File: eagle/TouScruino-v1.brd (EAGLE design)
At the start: 53.3 x 59.7 mm, 47 parts, among them J1 AVR_ISP, Q1 8MHz, Q2 MMBT2222, Q3 8MHz, U1 ATMEGA1284P, U3 ARDUINO_SHIELD, U4 MCP73831, U5 MIC5209-3.3YS, X1 USBSMD

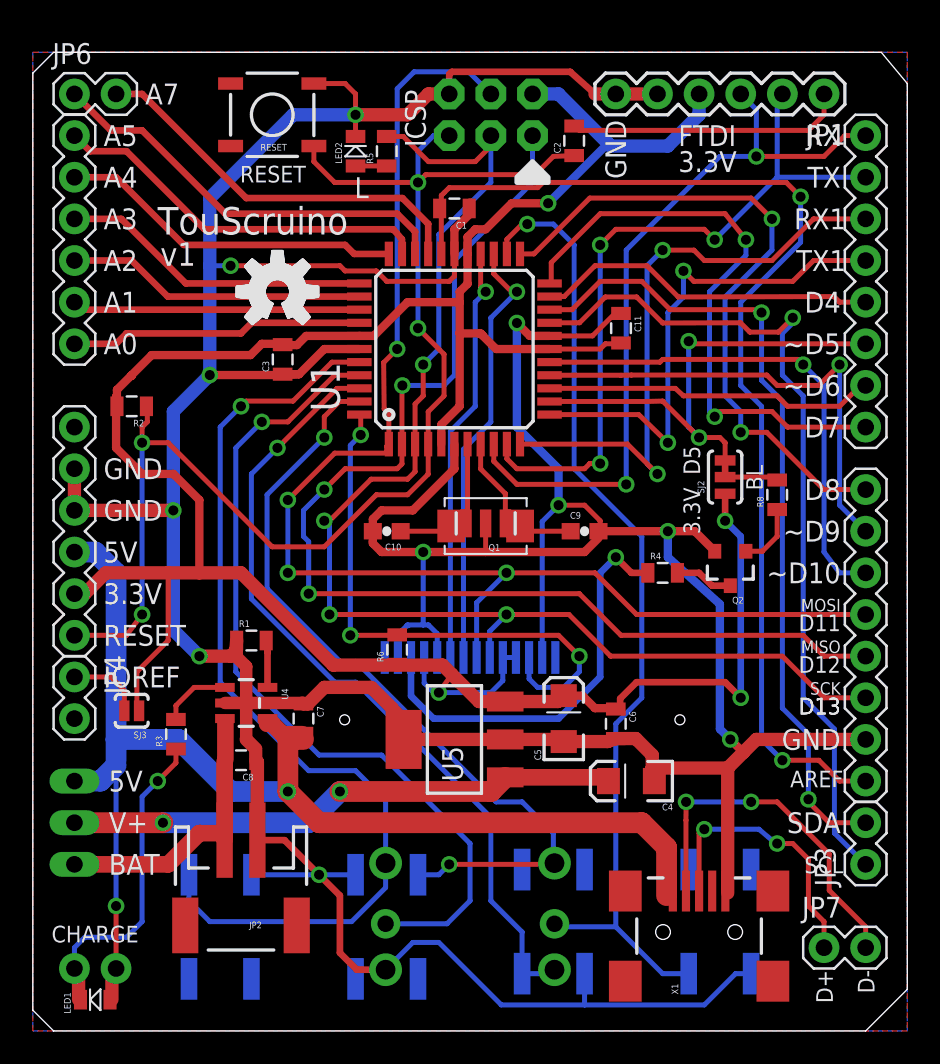
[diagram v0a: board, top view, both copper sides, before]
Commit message: 
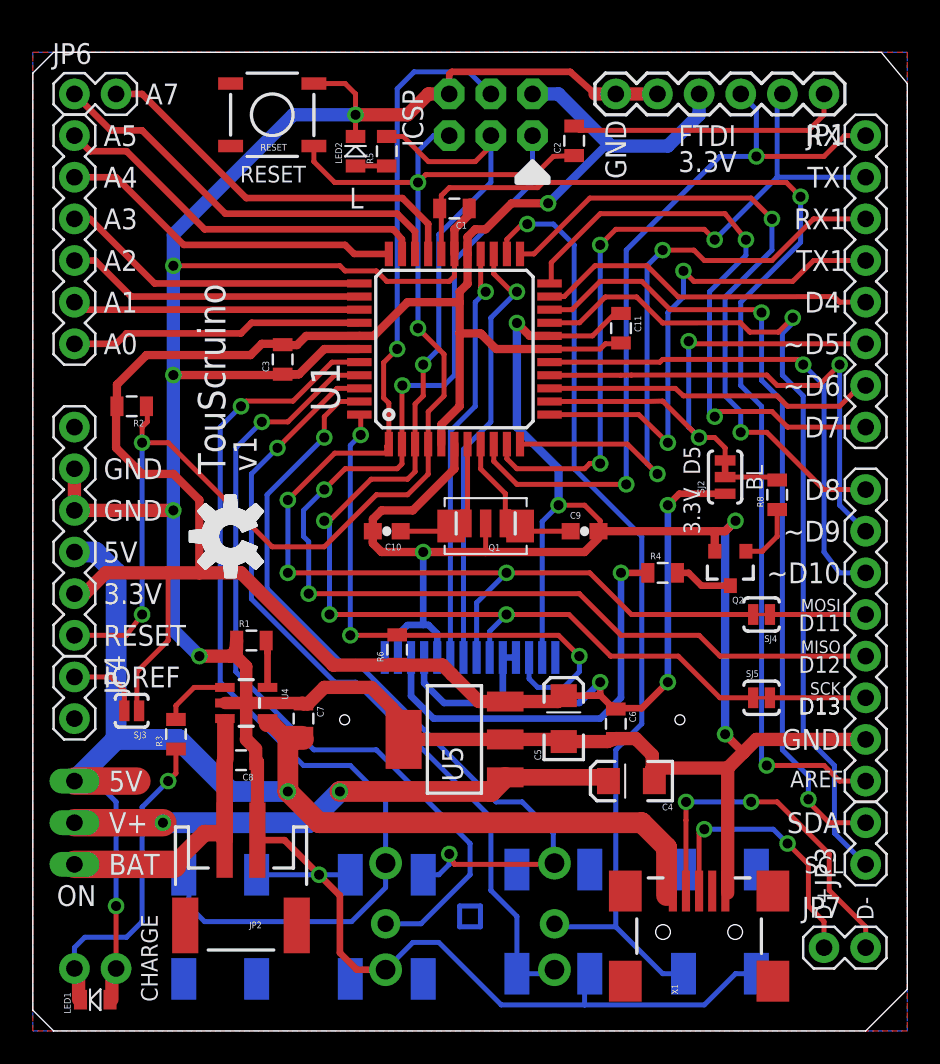
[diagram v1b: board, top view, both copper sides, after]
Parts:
- added SJ4, SJ5: (no value), SparkFun:SJ_2S-TRACE
- moved U$3 15.2 mm to (12.1, 30.2), turned to 90 degrees
- moved U$5 15.2 mm to (12.1, 30.2), turned to 90 degrees
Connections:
- net D18 renamed D18/SS
- new net N$6: SJ4.1, U3.D11
- new net N$9: SJ5.2, U3.D13
- net D11/MOSI: now also SJ4.2; no longer U3.D11
- net D13/SCK: now also SJ5.1; no longer U3.D13
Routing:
- net D13/SCK: track 80.9 -> 74.0 mm
- net D11/MOSI: track 83.3 -> 76.5 mm
- net GND: track 323.8 -> 329.9 mm
- net N$9: track 0.00 -> 5.84 mm
- net N$6: track 0.00 -> 5.84 mm
- net 3.3V: track 170.8 -> 175.1 mm
- net VUSB: track 77.6 -> 81.0 mm
- net D15/RIGHT: track 50.9 -> 49.9 mm
- net AREF: track 68.9 -> 69.6 mm
- net D17/PLUS: track 48.6 -> 49.3 mm
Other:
- board text added: "ON"

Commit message: 
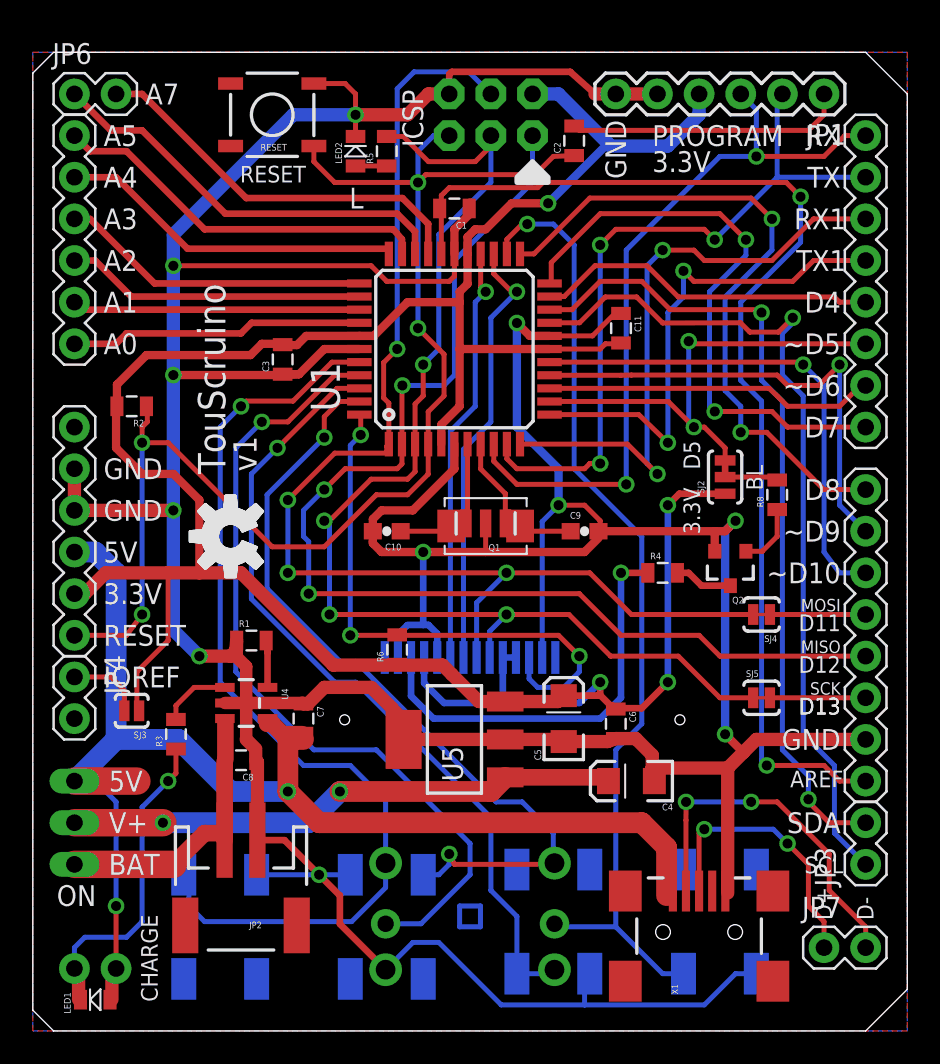
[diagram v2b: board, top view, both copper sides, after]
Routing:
- net GND: track 329.9 -> 328.9 mm
- net 3.3V: track 175.1 -> 174.5 mm
- net D5/PWM1: track 29.7 -> 29.2 mm
- net D7: track 36.8 -> 36.3 mm
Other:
- outline, holes or cut-outs redrawn
- board text added: "PROGRAM 3.3V"
- board text removed: "FTDI 3.3V"
